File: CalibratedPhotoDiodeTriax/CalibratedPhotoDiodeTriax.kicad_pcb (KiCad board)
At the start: 2 copper layers, 50.8 x 50.8 mm, 2 parts, among them J1 TO-5 Photodiode Socket: Conn_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, J2 CBJ70 Triax Throughhole Conne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

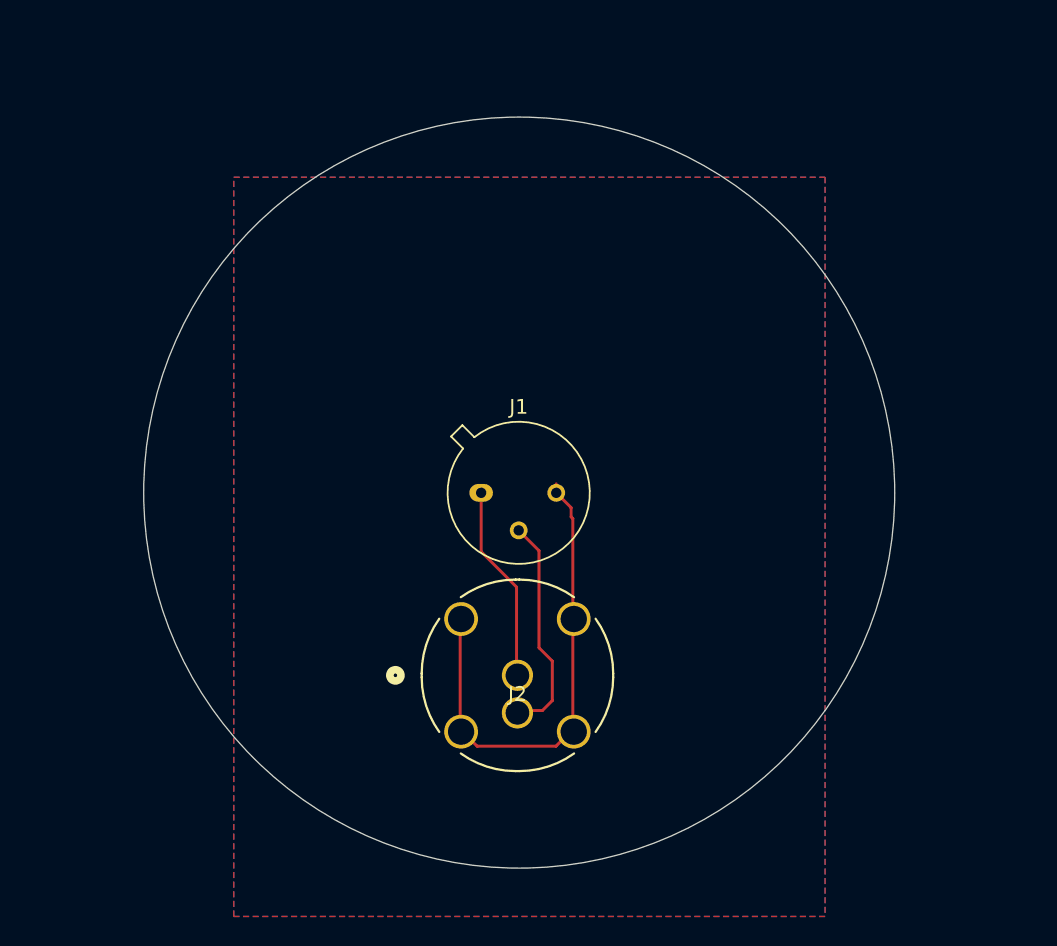
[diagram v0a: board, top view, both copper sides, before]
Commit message: Revision
Removed user drawing from triax pin. Increased ground pour to entire region. Removed redundant traces between ground pins. Decreased triax force/shield thru hole and decreased ground pour clearance to surround pins. Added circular aperture to pins.
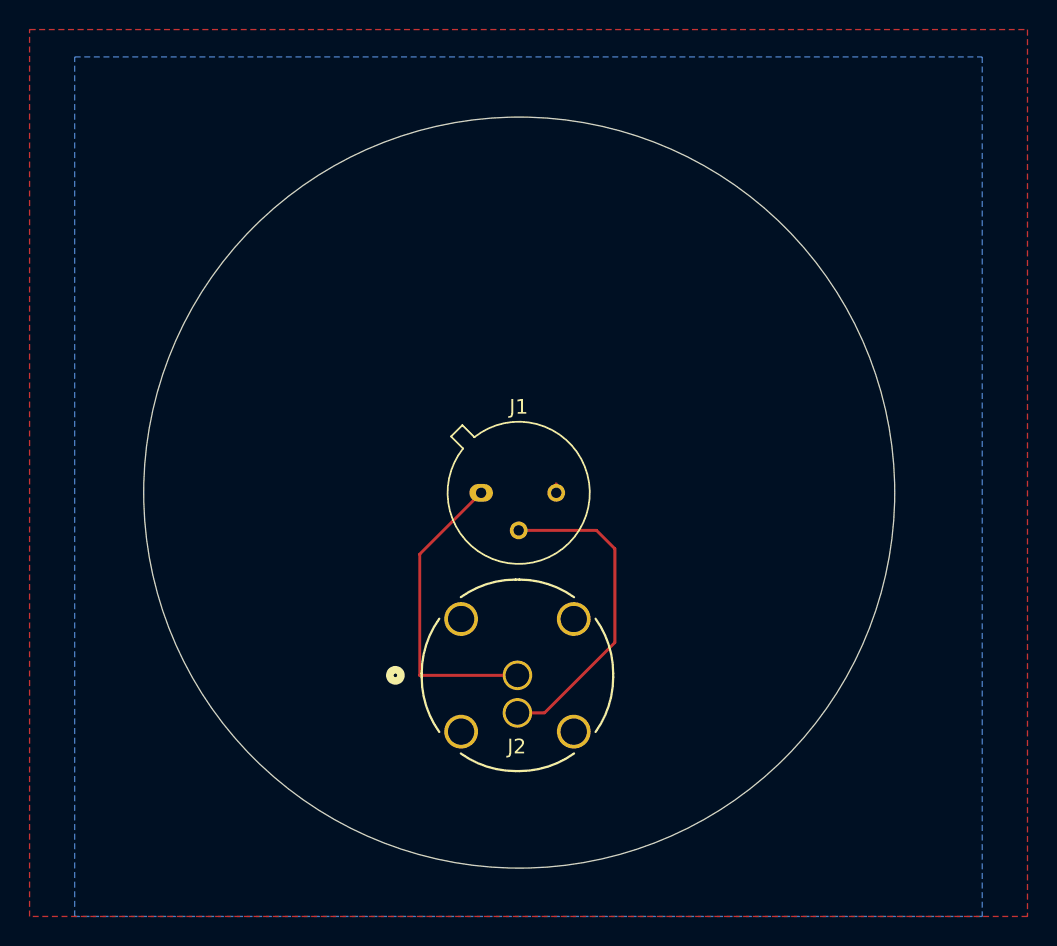
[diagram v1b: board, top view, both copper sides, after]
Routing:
- net GND: track 33.3 -> 0.61 mm
- net Net-(J1-Pin_1): track 13.2 -> 20.7 mm
- net Net-(J1-Pin_2): track 15.2 -> 21.9 mm
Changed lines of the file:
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@@
 		(tags "CBJ70 ")
 		(property "Reference" "J2"
-			(at 0 1.27 0)
+			(at -0.05 4.82 0)
 			(unlocked yes)
 			(layer "F.SilkS")
@@
 		)
 		(property "Value" "CBJ70 Triax Throughhole Connector"
-			(at 0 8.19 0)
+			(at 0 7.7 0)
 			(unlocked yes)
 			(layer "F.Fab")
@@
 		)
 		(fp_text user "${REFERENCE}"
-			(at 0 1.27 0)
+			(at -0.07 4.8 0)
 			(unlocked yes)
 			(layer "F.Fab")
@@
 		(pad "1" thru_hole circle
 			(at 0 0)
-			(size 2.1082 2.1082)
-			(drill 1.6002)
+			(size 2 2)
+			(drill 1.6)
 			(layers "*.Cu" "*.Mask")
 			(remove_unused_layers no)
@@
 		(pad "2" thru_hole circle
 			(at 0 2.54)
-			(size 2.1082 2.1082)
-			(drill 1.6002)
+			(size 2 2)
+			(drill 1.6)
 			(layers "*.Cu" "*.Mask")
 			(remove_unused_layers no)
@@
 			(size 2.286 2.286)
 			(drill 1.778)
-			(layers "*.Cu" "*.Mask" "Dwgs.User")
+			(layers "*.Cu" "*.Mask")
 			(remove_unused_layers no)
 			(net 3 "GND")
@@
 	)
 	(gr_circle
+		(center 159.779612 71.39)
+		(end 160.479612 70.341869)
+		(stroke
+			(width 0.1)
+			(type solid)
+		)
+		(fill no)
+		(layer "F.Mask")
+	)
+	(gr_circle
+		(center 159.69 81.179612)
+		(end 160.39 80.131481)
+		(stroke
+			(width 0.1)
+			(type solid)
+		)
+		(fill no)
+		(layer "F.Mask")
+	)
+	(gr_circle
+		(center 157.239612 68.848895)
+		(end 157.939612 67.800764)
+		(stroke
+			(width 0.1)
+			(type solid)
+		)
+		(fill no)
+		(layer "F.Mask")
+	)
+	(gr_circle
+		(center 159.69 83.719612)
+		(end 160.39 82.671481)
+		(stroke
+			(width 0.1)
+			(type solid)
+		)
+		(fill no)
+		(layer "F.Mask")
+	)
+	(gr_circle
+		(center 159.779612 71.38)
+		(end 160.479612 70.331869)
+		(stroke
+			(width 0.1)
+			(type solid)
+		)
+		(fill no)
+		(layer "B.Mask")
+	)
+	(gr_circle
+		(center 157.239612 68.848895)
+		(end 157.939612 67.800764)
+		(stroke
+			(width 0.1)
+			(type solid)
+		)
+		(fill no)
+		(layer "B.Mask")
+	)
+	(gr_circle
+		(center 159.69 83.719612)
+		(end 160.39 82.671481)
+		(stroke
+			(width 0.1)
+			(type default)
+		)
+		(fill no)
+		(layer "B.Mask")
+	)
+	(gr_circle
+		(center 159.69 81.179612)
+		(end 160.39 80.131481)
+		(stroke
+			(width 0.1)
+			(type default)
+		)
+		(fill no)
+		(layer "B.Mask")
+	)
+	(gr_circle
 		(center 159.81 68.83)
 		(end 185.21 68.83)
@@
 	)
 	(segment
-		(start 157.235 72.825)
-		(end 159.63 75.22)
+		(start 153.08 72.9998)
+		(end 153.08 81.19)
 		(width 0.2)
 		(layer "F.Cu")
@@
 	(segment
 		(start 157.235 68.8448)
-		(end 157.235 72.825)
+		(end 153.08 72.9998)
 		(width 0.2)
 		(layer "F.Cu")
@@
 	)
 	(segment
-		(start 159.63 75.22)
-		(end 159.63 81.03)
+		(start 153.08 81.19)
+		(end 159.69 81.19)
 		(width 0.2)
 		(layer "F.Cu")
 		(net 1)
-	)
-	(segment
-		(start 162.05 82.9)
-		(end 161.38 83.57)
-		(width 0.2)
-		(layer "F.Cu")
-		(net 2)
-	)
-	(segment
-		(start 162.05 80.23)
-		(end 162.05 82.9)
-		(width 0.2)
-		(layer "F.Cu")
-		(net 2)
-	)
-	(segment
-		(start 161.38 83.57)
-		(end 159.63 83.57)
-		(width 0.2)
-		(layer "F.Cu")
-		(net 2)
 	)
 	(segment
 		(start 159.775 71.3848)
-		(end 161.15 72.7598)
+		(end 165.0348 71.3848)
 		(width 0.2)
 		(layer "F.Cu")
@@
 	)
 	(segment
-		(start 161.15 79.33)
-		(end 162.05 80.23)
+		(start 161.52 83.73)
+		(end 159.69 83.73)
 		(width 0.2)
 		(layer "F.Cu")
@@
 	)
 	(segment
-		(start 161.15 72.7598)
-		(end 161.15 79.33)
+		(start 166.28 72.63)
+		(end 166.28 78.97)
 		(width 0.2)
 		(layer "F.Cu")
@@
 	)
 	(segment
-		(start 163.44 84.84)
-		(end 162.297 85.983)
+		(start 166.28 78.97)
+		(end 161.52 83.73)
 		(width 0.2)
 		(layer "F.Cu")
-		(net 3)
+		(net 2)
 	)
 	(segment
-		(start 163.44 70.59)
-		(end 163.44 77.22)
+		(start 165.0348 71.3848)
+		(end 166.28 72.63)
 		(width 0.2)
 		(layer "F.Cu")
-		(net 3)
+		(net 2)
 	)
 	(segment
@@
 		(net 3)
 	)
-	(segment
-		(start 162.297 85.983)
-		(end 156.963 85.983)
-		(width 0.2)
-		(layer "F.Cu")
-		(net 3)
-	)
-	(segment
-		(start 163.32 70.47)
-		(end 163.44 70.59)
-		(width 0.2)
-		(layer "F.Cu")
-		(net 3)
-	)
-	(segment
-		(start 156.963 85.983)
-		(end 155.82 84.84)
-		(width 0.2)
-		(layer "F.Cu")
-		(net 3)
-	)
-	(segment
-		(start 163.32 69.8498)
-		(end 163.32 70.47)
-		(width 0.2)
-		(layer "F.Cu")
-		(net 3)
-	)
-	(segment
-		(start 162.315 68.8448)
-		(end 163.32 69.8498)
-		(width 0.2)
-		(layer "F.Cu")
-		(net 3)
-	)
-	(segment
-		(start 155.82 84.84)
-		(end 155.82 77.22)
-		(width 0.2)
-		(layer "F.Cu")
-		(net 3)
-	)
-	(segment
-		(start 163.44 77.22)
-		(end 163.44 84.84)
-		(width 0.2)
-		(layer "F.Cu")
-		(net 3)
-	)
 	(zone
 		(net 3)
@@
 		(hatch edge 0.5)
 		(connect_pads
-			(clearance 0.5)
-		)
-		(min_thickness 0.25)
+			(clearance 0.05)
+		)
+		(min_thickness 0.1)
 		(filled_areas_thickness no)
 		(fill yes
@@
 		(polygon
 			(pts
-				(xy 140.5 47.5) (xy 180.5 47.5) (xy 180.5 97.5) (xy 140.5 97.5)
+				(xy 126.69 37.51) (xy 194.19 37.51) (xy 194.19 97.5) (xy 126.69 97.5)
 			)
 		)
@@
 		(priority 1)
 		(connect_pads
-			(clearance 0.5)
-		)
-		(min_thickness 0.25)
+			(clearance 0.05)
+		)
+		(min_thickness 0.1)
 		(filled_areas_thickness no)
 		(fill yes
@@
 		(polygon
 			(pts
-				(xy 140.5 47.5) (xy 180.5 47.5) (xy 180.5 97.5) (xy 140.5 97.5)
-			)
-		)
+				(xy 129.74 39.36) (xy 191.13 39.36) (xy 191.13 97.5) (xy 129.74 97.5)
+			)
+		)

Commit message: Trying to revise accessibility
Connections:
- J1 pad 2: Net-(J1-Pin_2) -> GND
- J1 pad 3: GND -> Net-(J1-Pin_3)
- J2 pad 2: Net-(J1-Pin_2) -> Net-(J1-Pin_3)
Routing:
- net GND: track 0.61 -> 47.6 mm
- net Net-(J1-Pin_2): track 21.9 -> 0.00 mm
- net Net-(J1-Pin_3): track 0.00 -> 18.3 mm
- net Net-(J1-Pin_1): track 20.7 -> 13.2 mm
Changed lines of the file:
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@@
 	(net 0 "")
 	(net 1 "Net-(J1-Pin_1)")
-	(net 2 "Net-(J1-Pin_2)")
+	(net 2 "Net-(J1-Pin_3)")
 	(net 3 "GND")
 	(footprint "KiCADv6:CONN_CBJ70_CIN"
@@
 		(tags "CBJ70 ")
 		(property "Reference" "J2"
-			(at -0.05 4.82 0)
+			(at 0 1.27 0)
 			(unlocked yes)
 			(layer "F.SilkS")
@@
 		)
 		(property "Value" "CBJ70 Triax Throughhole Connector"
-			(at 0 7.7 0)
+			(at 0 8.19 0)
 			(unlocked yes)
 			(layer "F.Fab")
@@
 		)
 		(fp_text user "${REFERENCE}"
-			(at -0.07 4.8 0)
+			(at 0 1.27 0)
 			(unlocked yes)
 			(layer "F.Fab")
@@
 		(pad "1" thru_hole circle
 			(at 0 0)
-			(size 2 2)
-			(drill 1.6)
+			(size 2.1082 2.1082)
+			(drill 1.6002)
 			(layers "*.Cu" "*.Mask")
 			(remove_unused_layers no)
@@
 		(pad "2" thru_hole circle
 			(at 0 2.54)
-			(size 2 2)
-			(drill 1.6)
+			(size 2.1082 2.1082)
+			(drill 1.6002)
 			(layers "*.Cu" "*.Mask")
 			(remove_unused_layers no)
-			(net 2 "Net-(J1-Pin_2)")
+			(net 2 "Net-(J1-Pin_3)")
 			(pinfunction "In2")
 			(pintype "passive")
@@
 			(size 2.286 2.286)
 			(drill 1.778)
-			(layers "*.Cu" "*.Mask")
+			(layers "*.Cu" "*.Mask" "Dwgs.User")
 			(remove_unused_layers no)
 			(net 3 "GND")
@@
 			(layers "*.Cu" "*.Mask")
 			(remove_unused_layers no)
-			(net 2 "Net-(J1-Pin_2)")
+			(net 3 "GND")
 			(pinfunction "Pin_2")
 			(pintype "passive")
@@
 			(layers "*.Cu" "*.Mask")
 			(remove_unused_layers no)
-			(net 3 "GND")
+			(net 2 "Net-(J1-Pin_3)")
 			(pinfunction "Pin_3")
 			(pintype "passive")
@@
 			)
 		)
-	)
-	(gr_circle
-		(center 159.779612 71.39)
-		(end 160.479612 70.341869)
-		(stroke
-			(width 0.1)
-			(type solid)
-		)
-		(fill no)
-		(layer "F.Mask")
-	)
-	(gr_circle
-		(center 159.69 81.179612)
-		(end 160.39 80.131481)
-		(stroke
-			(width 0.1)
-			(type solid)
-		)
-		(fill no)
-		(layer "F.Mask")
-	)
-	(gr_circle
-		(center 157.239612 68.848895)
-		(end 157.939612 67.800764)
-		(stroke
-			(width 0.1)
-			(type solid)
-		)
-		(fill no)
-		(layer "F.Mask")
-	)
-	(gr_circle
-		(center 159.69 83.719612)
-		(end 160.39 82.671481)
-		(stroke
-			(width 0.1)
-			(type solid)
-		)
-		(fill no)
-		(layer "F.Mask")
-	)
-	(gr_circle
-		(center 159.779612 71.38)
-		(end 160.479612 70.331869)
-		(stroke
-			(width 0.1)
-			(type solid)
-		)
-		(fill no)
-		(layer "B.Mask")
-	)
-	(gr_circle
-		(center 157.239612 68.848895)
-		(end 157.939612 67.800764)
-		(stroke
-			(width 0.1)
-			(type solid)
-		)
-		(fill no)
-		(layer "B.Mask")
-	)
-	(gr_circle
-		(center 159.69 83.719612)
-		(end 160.39 82.671481)
-		(stroke
-			(width 0.1)
-			(type default)
-		)
-		(fill no)
-		(layer "B.Mask")
-	)
-	(gr_circle
-		(center 159.69 81.179612)
-		(end 160.39 80.131481)
-		(stroke
-			(width 0.1)
-			(type default)
-		)
-		(fill no)
-		(layer "B.Mask")
 	)
 	(gr_circle
@@
 	)
 	(segment
-		(start 153.08 72.9998)
-		(end 153.08 81.19)
+		(start 157.235 72.825)
+		(end 159.63 75.22)
 		(width 0.2)
 		(layer "F.Cu")
@@
 	(segment
 		(start 157.235 68.8448)
-		(end 153.08 72.9998)
+		(end 157.235 72.825)
 		(width 0.2)
 		(layer "F.Cu")
@@
 	)
 	(segment
-		(start 153.08 81.19)
-		(end 159.69 81.19)
+		(start 159.63 75.22)
+		(end 159.63 81.03)
 		(width 0.2)
 		(layer "F.Cu")
@@
 	)
 	(segment
-		(start 159.775 71.3848)
-		(end 165.0348 71.3848)
+		(start 162.5 80.5)
+		(end 162.5 82.5)
 		(width 0.2)
 		(layer "F.Cu")
@@
 	)
 	(segment
-		(start 161.52 83.73)
-		(end 159.69 83.73)
+		(start 162.315 74.185)
+		(end 161.5 75)
 		(width 0.2)
 		(layer "F.Cu")
@@
 	)
 	(segment
-		(start 166.28 72.63)
-		(end 166.28 78.97)
+		(start 161.5 75)
+		(end 161.5 79.5)
 		(width 0.2)
 		(layer "F.Cu")
@@
 	)
 	(segment
-		(start 166.28 78.97)
-		(end 161.52 83.73)
-		(width 0.2)
-		(layer "F.Cu")
-		(net 2)
-	)
-	(segment
-		(start 165.0348 71.3848)
-		(end 166.28 72.63)
+		(start 161.5 79.5)
+		(end 162.5 80.5)
 		(width 0.2)
 		(layer "F.Cu")
@@
 		(width 0.2)
 		(layer "F.Cu")
+		(net 2)
+	)
+	(segment
+		(start 162.5 82.5)
+		(end 161.27 83.73)
+		(width 0.2)
+		(layer "F.Cu")
+		(net 2)
+	)
+	(segment
+		(start 161.27 83.73)
+		(end 159.69 83.73)
+		(width 0.2)
+		(layer "F.Cu")
+		(net 2)
+	)
+	(segment
+		(start 162.315 68.8448)
+		(end 162.315 74.185)
+		(width 0.2)
+		(layer "F.Cu")
+		(net 2)
+	)
+	(segment
+		(start 159.775 71.3848)
+		(end 159.775 67.275)
+		(width 0.2)
+		(layer "F.Cu")
+		(net 3)
+	)
+	(segment
+		(start 158.5 66)
+		(end 156 66)
+		(width 0.2)
+		(layer "F.Cu")
+		(net 3)
+	)
+	(segment
+		(start 154.5 67.5)
+		(end 154.5 74)
+		(width 0.2)
+		(layer "F.Cu")
+		(net 3)
+	)
+	(segment
+		(start 161.5 87)
+		(end 163.5 85)
+		(width 0.2)
+		(layer "F.Cu")
+		(net 3)
+	)
+	(segment
+		(start 163.5 85)
+		(end 166 82.5)
+		(width 0.2)
+		(layer "F.Cu")
+		(net 3)
+	)
+	(segment
+		(start 155.88 75.38)
+		(end 155.88 77.38)
+		(width 0.2)
+		(layer "F.Cu")
+		(net 3)
+	)
+	(segment
+		(start 155.88 77.38)
+		(end 155.88 85)
+		(width 0.2)
+		(layer "F.Cu")
+		(net 3)
+	)
+	(segment
+		(start 159.775 67.275)
+		(end 158.5 66)
+		(width 0.2)
+		(layer "F.Cu")
+		(net 3)
+	)
+	(segment
+		(start 154.5 74)
+		(end 155.88 75.38)
+		(width 0.2)
+		(layer "F.Cu")
+		(net 3)
+	)
+	(segment
+		(start 156 66)
+		(end 154.5 67.5)
+		(width 0.2)
+		(layer "F.Cu")
+		(net 3)
+	)
+	(segment
+		(start 166 79.88)
+		(end 163.5 77.38)
+		(width 0.2)
+		(layer "F.Cu")
+		(net 3)
+	)
+	(segment
+		(start 155.88 85)
+		(end 157.88 87)
+		(width 0.2)
+		(layer "F.Cu")
+		(net 3)
+	)
+	(segment
+		(start 166 82.5)
+		(end 166 79.88)
+		(width 0.2)
+		(layer "F.Cu")
+		(net 3)
+	)
+	(segment
+		(start 157.88 87)
+		(end 161.5 87)
+		(width 0.2)
+		(layer "F.Cu")
 		(net 3)
 	)
@@
 		(hatch edge 0.5)
 		(connect_pads
-			(clearance 0.05)
-		)
-		(min_thickness 0.1)
+			(clearance 0.5)
+		)
+		(min_thickness 0.25)
 		(filled_areas_thickness no)
 		(fill yes
@@
 		(polygon
 			(pts
-				(xy 126.69 37.51) (xy 194.19 37.51) (xy 194.19 97.5) (xy 126.69 97.5)
+				(xy 140.5 47.5) (xy 180.5 47.5) (xy 180.5 97.5) (xy 140.5 97.5)
 			)
 		)
@@
 		(priority 1)
 		(connect_pads
-			(clearance 0.05)
-		)
-		(min_thickness 0.1)
+			(clearance 0.5)
+		)
+		(min_thickness 0.25)
 		(filled_areas_thickness no)
 		(fill yes
@@
 		(polygon
 			(pts
-				(xy 129.74 39.36) (xy 191.13 39.36) (xy 191.13 97.5) (xy 129.74 97.5)
-			)
-		)
+				(xy 140.5 47.5) (xy 180.5 47.5) (xy 180.5 97.5) (xy 140.5 97.5)
+			)
+		)
